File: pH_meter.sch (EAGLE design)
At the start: 45 parts, among them IC1 W25Q64JVXGIQ, J3 TF-123-ARP9HXX, U1 RP2040, U3 MIC5504-3.3YM5_TR

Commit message: Daily check-in
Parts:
- removed CONN1: GT-USB_8012A, GT_USB-8012A:GT-USB_8012A
- added C18, C22, C23, C29, C32, C33: 0.1uF, SparkFun-Capacitors:0.1UF-0603-25V-5%
- added C24, C31: 0.1uF, SparkFun-Capacitors:0.1UF-0603-50V-10%-X7R-WE
- added C25, C26, C28, C30: 10uF, SparkFun-Capacitors:10UF-0603-6.3V-20%
- added C27: 0.1uF, SparkFun-Capacitors:0.1UF-0402-16V-10%
- added J1: TYPE-C-31-M-12, TYPE-C-31-M-12:TYPE-C-31-M-12
- added J4, J5: 60312202114511, 60312202114511:60312202114511
- added R11: 10k, SparkFun-Resistors:10KOHM-0603-1/10W-1%
- added R12, R13: 2.2k, SparkFun-Resistors:2.2KOHM-0603-1/10W-1%
- added R15, R16, R17, R18: (no value), SparkFun-Resistors:RESISTOR0402
- added R9: 16.9k, SparkFun-Resistors:16.2KOHM-0603-1/10W-1%
- added U$1, U$2: PH-OEM, pH-OEM:PH-OEM
- added U2: BME280, BME280:BME280
- added U4: ADM3260ARSZ, ADM3260ARSZ:ADM3260ARSZ
- added U5: SFH6325-X017T, SFH6325-X017T:SFH6325-X017T
- C12, C13: device SparkFun-Capacitors:0.1UF-0402-16V-10% -> SparkFun-Capacitors:0.1UF-0603-25V-(+80/-20%)
- C14, C15: device OPL_Capacitor:CERAMIC-10UF-6.3V-20%-X5R(0402) -> SparkFun-Capacitors:10UF-0603-6.3V-20%
- C19: device SparkFun-Capacitors:0.1UF-0402-16V-10% -> SparkFun-Capacitors:0.1UF-0603-25V-5%
- L1: value 2.2nH -> LQW18AN2N2D10D; device SparkFun-Coils:INDUCTOR-0402-3.9NH -> LQW18AN2N2D10D:LQW18AN2N2D10D
- R1, R2: value 27 -> (none)
- R10: value 330 -> (none)
- R14: value 1K -> (none)
- R3, R8: value 5.1K -> 5.1k; device SparkFun-Resistors:RESISTOR0402 -> SparkFun-Resistors:5.1KOHM5.1KOHM-0603-1/10W-1%
- R4: value DNF -> (none)
- R5: value 10K -> (none)
- R6, R7: value 2.2K -> 2.2k; device SparkFun-Resistors:RESISTOR0402 -> SparkFun-Resistors:2.2KOHM-0603-1/10W-1%
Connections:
- new net GND-ISO: C24.2, C26.2, C30.2, C31.2, C32.2, C33.2, R11.1, U$1.GND, U$2.GND, U4.GNDISO, U5.C1, U5.C2
- new net INT_MOD1: R15.1, U1.GPIO0, U5.C1(VO1)
- new net INT_MOD1ISO: R18.1, U$2.INT
- new net INT_MOD2: R16.1, U1.GPIO1, U5.C2(VO2)
- new net INT_MOD2ISO: R17.1, U$1.INT
- new net N$2: R11.2, R9.1, U4.VSEL
- new net N$5: J1.CC2, R8.2
- new net N$8: R18.2, U5.A1
- new net PDIS: U1.GPIO20, U4.PDIS
- new net PROBE: J4.1, U$2.PRB
- new net PROBE2: J5.1, U$1.PRB
- new net PROBE2_GND: J5.2, U$1.PRB_GND
- new net PROBE_GND: J4.2, U$2.PRB_GND
- new net SCL_ISO: R13.1, U$1.SCL, U$2.SCL, U4.SCL1
- new net SDA_ISO: R12.1, U$1.SDA, U$2.SDA, U4.SDA1
- new net VCC-ISO: C24.1, C26.1, C30.1, C31.1, C32.1, C33.1, R12.2, R13.2, R9.2, U$1.VCC, U$2.VCC, U4.VDDISO, U4.VISO
- net 3.3V: now also C18.1, C22.1, C27.2, C28.1, C29.1, R15.2, R16.2, U2.CSB, U2.VDD, U2.VDDIO, U4.VDDP, U5.C(VCC)
- net GND: now also C18.2, C22.2, C23.2, C25.2, C27.1, C28.2, C29.2, J1.GND, J1.SHIELD, U2.GND, U2.SDO, U4.GNDP, U5.E(GND); no longer CONN1.GND, CONN1.SHIELD
- net N$3: now also J1.CC1; no longer CONN1.CC1
- net N$7: now also R17.2, U5.A2; no longer CONN1.CC2, R8.2
- net N$9: now also J1.VBUS; no longer CONN1.VBUS
- net SCL: now also U2.SCK, U4.SCL2
- net SDA: now also U2.SDI, U4.SDA2
- net USB_N: now also J1.DN1, J1.DN2; no longer CONN1.DN1, CONN1.DN2
- net USB_P: now also J1.DP1, J1.DP2; no longer CONN1.DP1, CONN1.DP2
- net V_USB: now also C23.1, C25.1, U4.VIN
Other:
- moved on the sheet: C12, C13, C16, C17, C19, IC1, J2, J3, L1, LED1, R4, R5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

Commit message: Partial component placement
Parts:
- removed D2: BLUE-0402, OPL_Optoelectronics:SMD-LED-CLEAR-BLUE(0402)
- added D1: (no value), SparkFun-LED:LED0603
- C1, C10, C11, C16, C17, C2, C27, C5, C6, C7, C8, C9: device SparkFun-Capacitors:0.1UF-0402-16V-10% -> SparkFun-Capacitors:0.1UF-0603-25V-(+80/-20%)
- C20, C21: value 33pf -> 33pF; device OPL_Capacitor:CERAMIC-33PF-50V-5%-NPO(0402) -> SparkFun-Capacitors:33PF-0603-50V-5%
- C3, C4: device SparkFun-Capacitors:1.0UF-0402-16V-10% -> SparkFun-Capacitors:1.0UF-0603-16V-10%
- C33: SPICEPREFIX C -> (none)
- R1, R2: value (none) -> 27; device SparkFun-Resistors:RESISTOR0402 -> SparkFun-Resistors:27OHM-0603-1/10W-1%
- R10, R17, R18: value (none) -> 100; device SparkFun-Resistors:RESISTOR0402 -> SparkFun-Resistors:100OHM-0603-1/10W-1%
- R14, R15, R16, R5: value (none) -> 1k; device SparkFun-Resistors:RESISTOR0402 -> SparkFun-Resistors:1KOHM-0603-1/10W-1%
- R4: device SparkFun-Resistors:RESISTOR0402 -> SparkFun-Resistors:RESISTOR0603
- R9: value 16.9k -> 16.2k
- U$1: SPICEPREFIX X -> (none)
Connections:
- removed net INT_ZMOD4510: U1.GPIO22
- removed net RES_ZMOD4510: U1.GPIO21
- net GND: now also D1.C; no longer D2.-
- net N$1: now also D1.A; no longer D2.+
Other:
- moved on the sheet: C12, C13, C14, C15, C18, C19, C22, C23, C24, C25, C26, C28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

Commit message: Generated gerbers
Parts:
- added C34: 0.1uF, SparkFun-Capacitors:0.1UF-0603-25V-(+80/-20%)
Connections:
- net 3.3V: now also C34.1
- net GND: now also C34.2

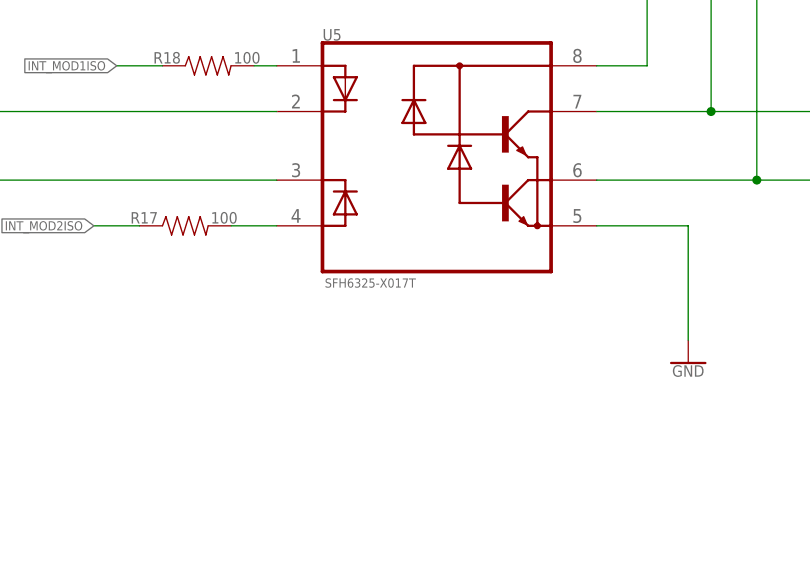
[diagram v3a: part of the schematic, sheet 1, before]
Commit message: Changes to accommodate BoM costs
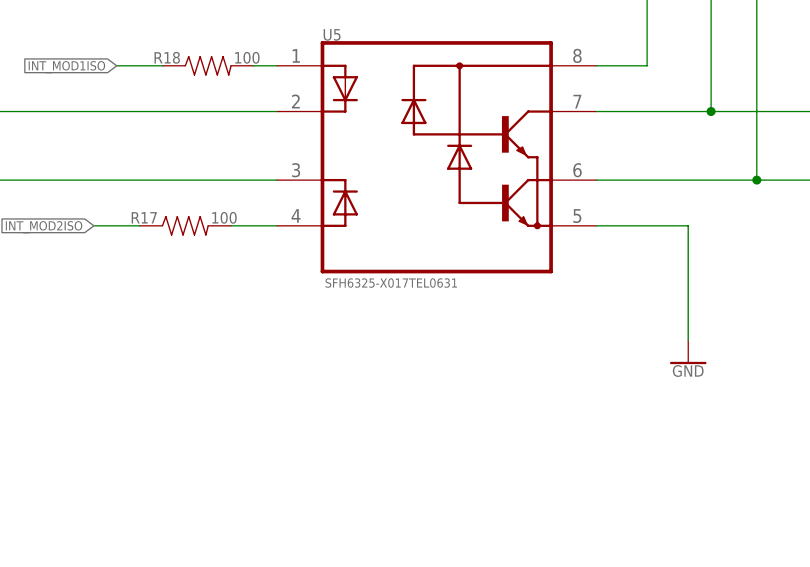
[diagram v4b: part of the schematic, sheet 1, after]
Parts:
- U5: value SFH6325-X017T -> SFH6325-X017TEL0631; device SFH6325-X017T:SFH6325-X017T -> SFH6325-X017T:SFH6325-X017TEL0631
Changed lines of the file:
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@@
 <part name="R13" library="SparkFun-Resistors" library_urn="urn:adsk.eagle:library:532" deviceset="2.2KOHM" device="-0603-1/10W-1%" package3d_urn="urn:adsk.eagle:package:41389018/1" override_package3d_urn="urn:adsk.eagle:package:44163370/2" override_package_urn="urn:adsk.eagle:footprint:39625/1" override_locally_modified="yes" value="2.2k"/>
 <part name="U$4" library="SparkFun-PowerSymbols" library_urn="urn:adsk.eagle:library:530" deviceset="VCC-ISO" device=""/>
-<part name="U5" library="SFH6325-X017T" deviceset="SFH6325-X017T" device="" override_package3d_urn="urn:adsk.eagle:package:44371568/2" override_package_urn="urn:adsk.eagle:footprint:44371569/1"/>
+<part name="U5" library="SFH6325-X017T" deviceset="SFH6325-X017T" device="EL0631" override_package3d_urn="urn:adsk.eagle:package:44371568/2" override_package_urn="urn:adsk.eagle:footprint:44371569/1" override_locally_modified="yes" value="SFH6325-X017TEL0631"/>
 <part name="GND-ISO3" library="SparkFun-PowerSymbols" library_urn="urn:adsk.eagle:library:530" deviceset="GND-ISO" device=""/>
 <part name="SUPPLY12" library="SparkFun-PowerSymbols" library_urn="urn:adsk.eagle:library:530" deviceset="3.3V" device=""/>
